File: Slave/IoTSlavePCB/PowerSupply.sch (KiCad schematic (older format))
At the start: 12 parts

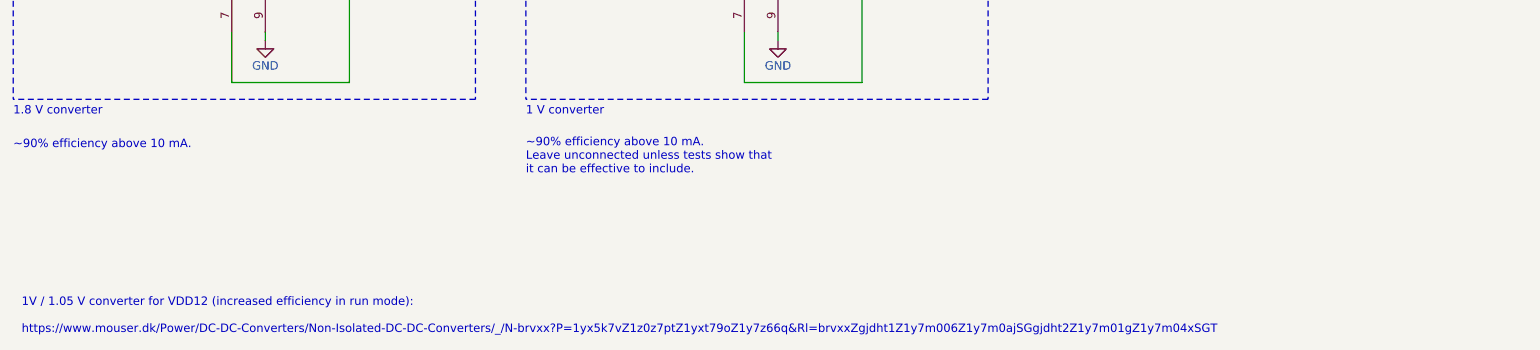
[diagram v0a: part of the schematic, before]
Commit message: Continued work on slaves. Added sensor and begun work on ZigBee transceiver.
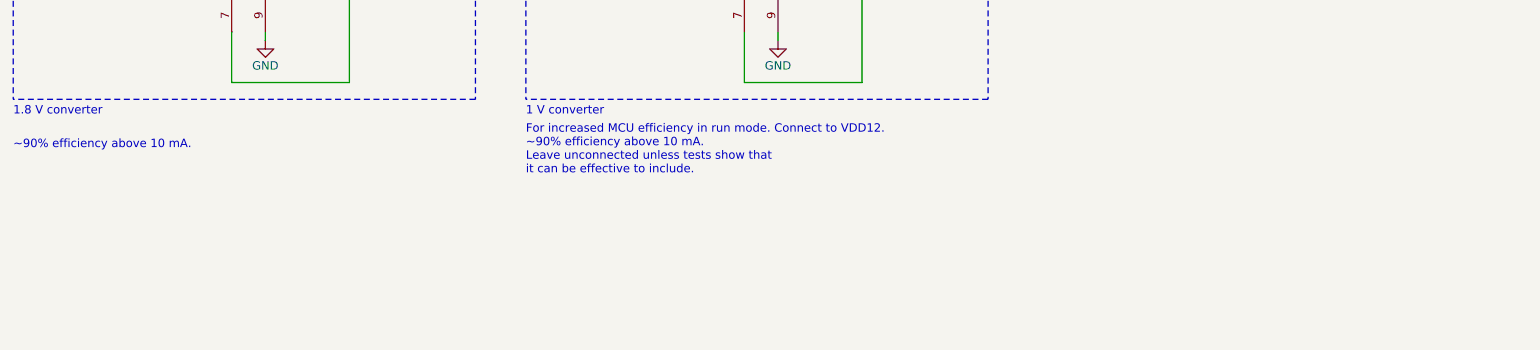
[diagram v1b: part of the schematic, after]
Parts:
- R?: footprint (none) -> Resistor_SMD:R_0603_1608Metric
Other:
- note added: "For increased MCU efficiency in run mode. Connect to VDD12.\n~~90% efficiency above 10 mA.\nLeave unconnected unless tests show that\nit can be effective to include."
- note removed: "1V / 1.05 V converter for VDD12 (increased efficiency in run mode):\n\nhttps://www.mouser.dk/Power/DC-DC-Converters/Non-Isolated-DC-DC-Converters/_/N-brvxx?P=1yx5k7vZ1z0z7ptZ1yxt79oZ1y7z66q&Rl=brvxxZgjdht1Z1y7m006Z1y7m0ajSGgjdht2Z1y7m01gZ1y7m04xSGT"
- note removed: "~~90% efficiency above 10 mA.\nLeave unconnected unless tests show that\nit can be effective to include."
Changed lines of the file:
@@
 F 0 "R?" H 2800 2000 50  0000 L CNN
 F 1 "25k" H 2800 1900 50  0000 L CNN
-F 2 "" V 2680 1950 50  0001 C CNN
+F 2 "Resistor_SMD:R_0603_1608Metric" V 2680 1950 50  0001 C CNN
 F 3 "~" H 2750 1950 50  0001 C CNN
 	1    2750 1950
@@
 Text Notes 1050 4850 0    50   ~ 0
 ~~90% efficiency above 10 mA.
-Text Notes 1100 5950 0    50   ~ 0
-1V / 1.05 V converter for VDD12 (increased efficiency in run mode):\n\nhttps://www.mouser.dk/Power/DC-DC-Converters/Non-Isolated-DC-DC-Converters/_/N-brvxx?P=1yx5k7vZ1z0z7ptZ1yxt79oZ1y7z66q&Rl=brvxxZgjdht1Z1y7m006Z1y7m0ajSGgjdht2Z1y7m01gZ1y7m04xSGT
 $Comp
 L Personal_ICs:MYRGP180100B21RA U?
@@
 Text Notes 4100 4650 0    50   ~ 0
 1 V converter
-Text Notes 4100 5000 0    50   ~ 0
-~~90% efficiency above 10 mA.\nLeave unconnected unless tests show that\nit can be effective to include.
 $Comp
 L Personal_ICs:MYRGP100100B21RA U?
@@
 	1    0    0    -1
 $EndComp
+Text Notes 4100 5000 0    50   ~ 0
+For increased MCU efficiency in run mode. Connect to VDD12.\n~~90% efficiency above 10 mA.\nLeave unconnected unless tests show that\nit can be effective to include.
 $EndSCHEMATC

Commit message: Finished slave schematics, including memory and Zigbee Transceiver. Further work on PCB, well underway.
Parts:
- added FB2: 1k @ 100 MHz, Inductor_SMD:L_0603_1608Metric, symbol Device:Ferrite_Bead_Small
- added FL1: ECMF02-4CMX8, Personal_Passives:ECMF024CMX8, symbol Personal_Passives:ECMF02-4CMX8
- added J2: 10118194-0001LF, Personal_Misc:10118194-0001LF, symbol Personal_Misc:10118194-0001LF
- added R3: 0R, Resistor_SMD:R_1206_3216Metric, symbol Device:R
- BT1: renamed from BT?; footprint (none) -> Personal_Misc:SMTU2430-LF
- C10, C11, C12, C13, C14, C9: renamed from C?; footprint (none) -> Capacitor_SMD:C_0805_2012Metric
- J3: renamed from J?; footprint (none) -> Connector_PinHeader_1.27mm:PinHeader_1x02_P1.27mm_Vertical
- gave numbers to parts that had none: 4
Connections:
- net GND: now also FL1.5 (GND), FL1.8 (GND), J2.5 (GND), R3.1
- net +5V: now reaches C9.1, J3.2 (Pin_2), U2.4 (VDD)
- net +5V: now also FB2.1, FL1.1 (VBUS)
- new net: FB2.2, J2.1 (VBUS)
- new net: FL1.2 (D-_I), J2.2 (D-)
- new net: FL1.3 (D+_I), J2.3 (D+)
- new net GND1: J2.S1 (Shield), R3.2
- new net USB_N: FL1.7 (D-_O)
- new net USB_P: FL1.6 (D+_O)
- no-connect marks 1 -> 3
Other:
- note added: "1 A"
- note added: "USB circuit"
- moved on the sheet: C13, C14, U4

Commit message: Change for clarity.
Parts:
- BT1: footprint Personal_Misc:SMTU2430-LF -> Personal_Misc:SMTU2450-LF
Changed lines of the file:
@@
 F 0 "BT1" H 4318 1896 50  0000 L CNN
 F 1 "LIR2450" H 4318 1805 50  0000 L CNN
-F 2 "Personal_Misc:SMTU2430-LF" V 4200 1860 50  0001 C CNN
+F 2 "Personal_Misc:SMTU2450-LF" V 4200 1860 50  0001 C CNN
 F 3 "~" V 4200 1860 50  0001 C CNN
 	1    4200 1800
